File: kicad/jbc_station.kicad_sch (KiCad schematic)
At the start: 120 parts, among them J1 PWR, J2 Conn_01x02, J3 Barcode, J4 Front panel, J5 Conn_01x03, J6 Conn_01x05, J7 Conn_01x04, J8 Conn_01x03, Q1 BSS138, Q2 BSS138, Q3 BSS138, U1 L78L05_SOT89, U10 STM32F401CCUx, U11 CH9141K, U2 LP2985-3.3, U3 ICL7660, U4 HT7463, U5 HT7463, U6 XC6206PxxxMR, U7 M24C64, U8 INA3221, U9 XC6206PxxxMR, Y1 Crystal, Y2 Crystal

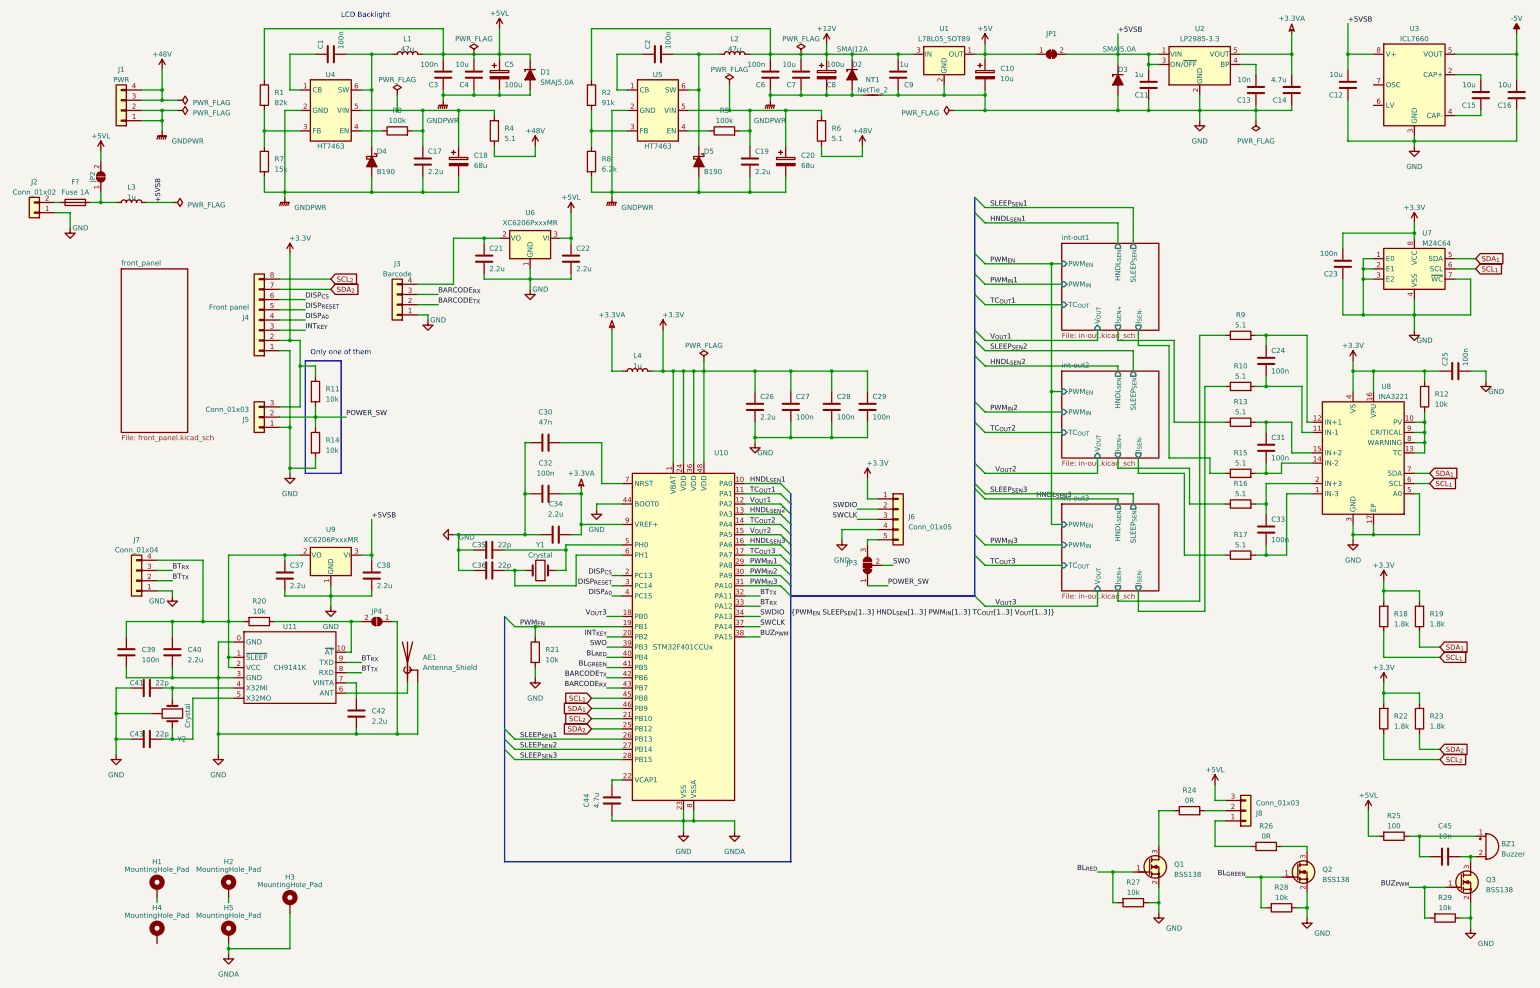
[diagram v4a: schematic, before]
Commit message: Sch: fix front panel labels naming
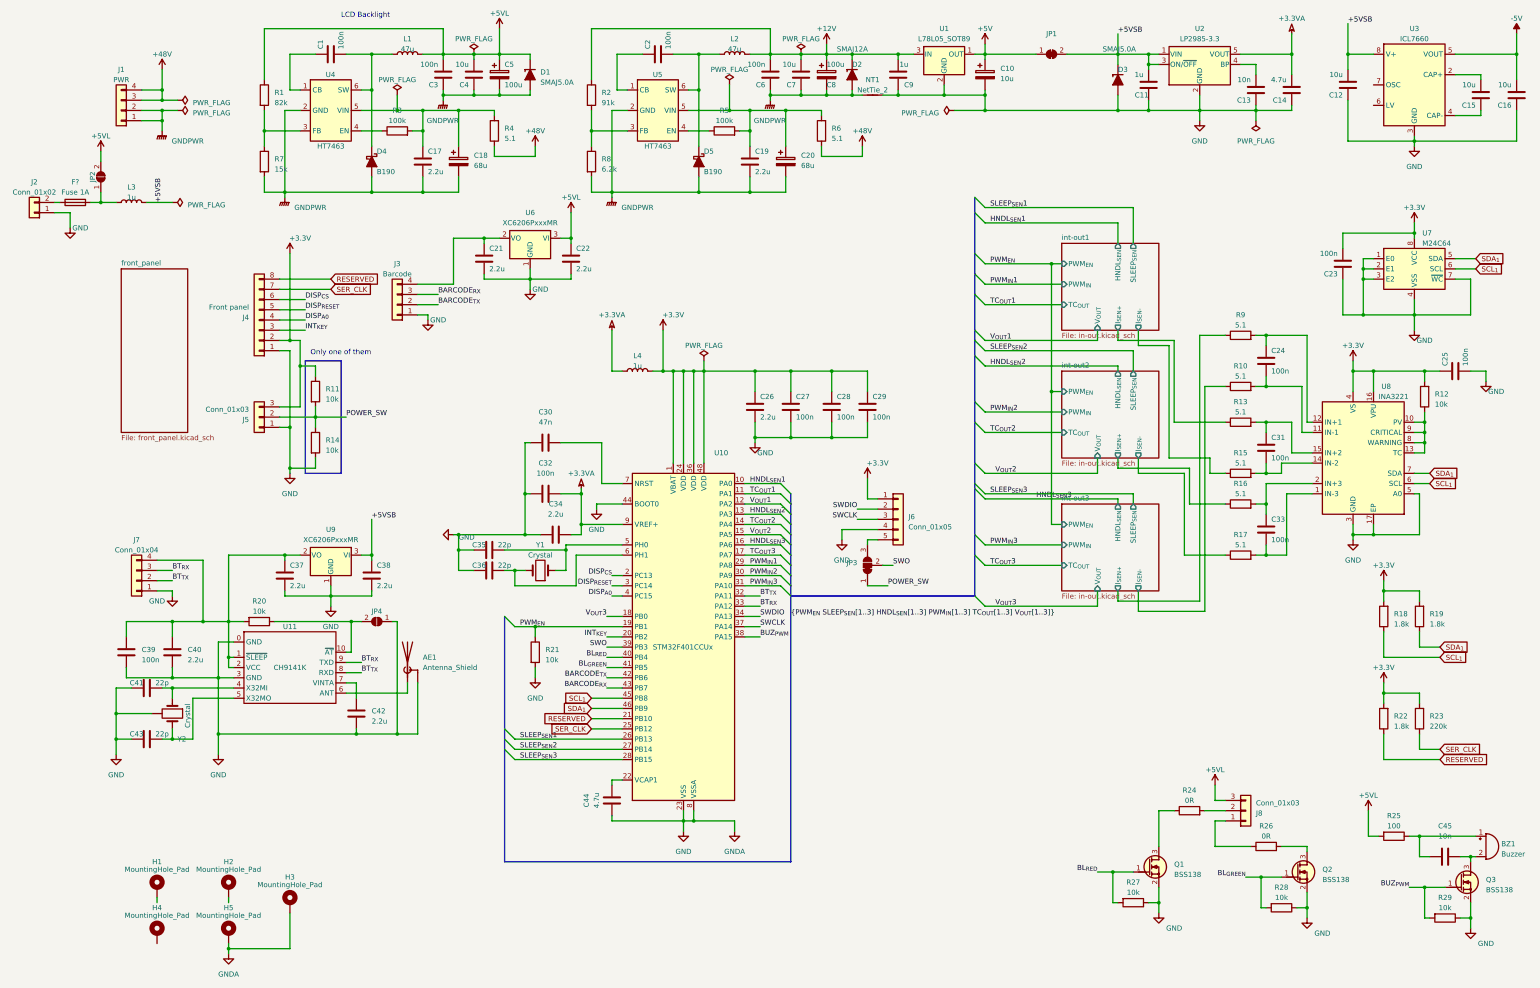
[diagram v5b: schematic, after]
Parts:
- R23: value 1.8k -> 220k
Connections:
- net SCL_{2} renamed RESERVED
- net SDA_{2} renamed SER_CLK
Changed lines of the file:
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@@
     )
   )
-  (global_label "SDA_{2}" (shape input) (at 377.19 201.93 0) (fields_autoplaced)
+  (global_label "SER_CLK" (shape input) (at 377.19 201.93 0) (fields_autoplaced)
     (effects (font (size 1.27 1.27)) (justify left))
-    (property "Intersheetrefs" "${INTERSHEET_REFS}" (at 384.5868 201.93 0)
+    (property "Intersheetrefs" "${INTERSHEET_REFS}" (at 388.26 201.93 0)
       (effects (font (size 1.27 1.27)) (justify left) hide)
     )
   )
-  (global_label "SCL_{2}" (shape input) (at 101.6 85.09 0) (fields_autoplaced)
+  (global_label "RESERVED" (shape input) (at 101.6 85.09 0) (fields_autoplaced)
     (effects (font (size 1.27 1.27)) (justify left))
-    (property "Intersheetrefs" "${INTERSHEET_REFS}" (at 108.9363 85.09 0)
+    (property "Intersheetrefs" "${INTERSHEET_REFS}" (at 114.0609 85.09 0)
       (effects (font (size 1.27 1.27)) (justify left) hide)
     )
   )
-  (global_label "SDA_{2}" (shape input) (at 101.6 87.63 0) (fields_autoplaced)
+  (global_label "SER_CLK" (shape input) (at 101.6 87.63 0) (fields_autoplaced)
     (effects (font (size 1.27 1.27)) (justify left))
-    (property "Intersheetrefs" "${INTERSHEET_REFS}" (at 108.9968 87.63 0)
+    (property "Intersheetrefs" "${INTERSHEET_REFS}" (at 112.67 87.63 0)
       (effects (font (size 1.27 1.27)) (justify left) hide)
     )
@@
     )
   )
-  (global_label "SCL_{2}" (shape input) (at 166.37 194.31 180) (fields_autoplaced)
+  (global_label "RESERVED" (shape input) (at 166.37 194.31 180) (fields_autoplaced)
     (effects (font (size 1.27 1.27)) (justify right))
-    (property "Intersheetrefs" "${INTERSHEET_REFS}" (at 159.0337 194.31 0)
+    (property "Intersheetrefs" "${INTERSHEET_REFS}" (at 153.9091 194.31 0)
       (effects (font (size 1.27 1.27)) (justify right) hide)
     )
   )
-  (global_label "SCL_{2}" (shape input) (at 377.19 204.47 0) (fields_autoplaced)
+  (global_label "RESERVED" (shape input) (at 377.19 204.47 0) (fields_autoplaced)
     (effects (font (size 1.27 1.27)) (justify left))
-    (property "Intersheetrefs" "${INTERSHEET_REFS}" (at 384.5263 204.47 0)
+    (property "Intersheetrefs" "${INTERSHEET_REFS}" (at 389.6509 204.47 0)
       (effects (font (size 1.27 1.27)) (justify left) hide)
     )
   )
-  (global_label "SDA_{2}" (shape input) (at 166.37 196.85 180) (fields_autoplaced)
+  (global_label "SER_CLK" (shape input) (at 166.37 196.85 180) (fields_autoplaced)
     (effects (font (size 1.27 1.27)) (justify right))
-    (property "Intersheetrefs" "${INTERSHEET_REFS}" (at 158.9732 196.85 0)
+    (property "Intersheetrefs" "${INTERSHEET_REFS}" (at 155.3 196.85 0)
       (effects (font (size 1.27 1.27)) (justify right) hide)
     )
@@
       (effects (font (size 1.27 1.27)) (justify right))
     )
-    (property "Value" "1.8k" (at 374.65 196.215 0)
+    (property "Value" "220k" (at 374.65 196.215 0)
       (effects (font (size 1.27 1.27)) (justify right))
     )
